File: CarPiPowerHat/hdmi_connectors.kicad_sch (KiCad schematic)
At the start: 2 parts, among them J1 HDMI_A_1.4, J6 1-84953-5

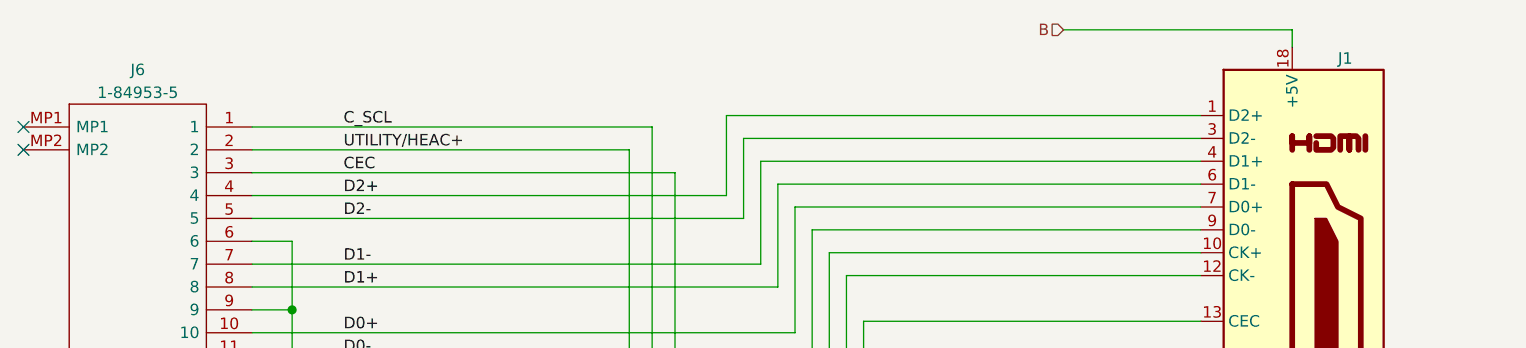
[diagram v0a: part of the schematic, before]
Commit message: updated layout
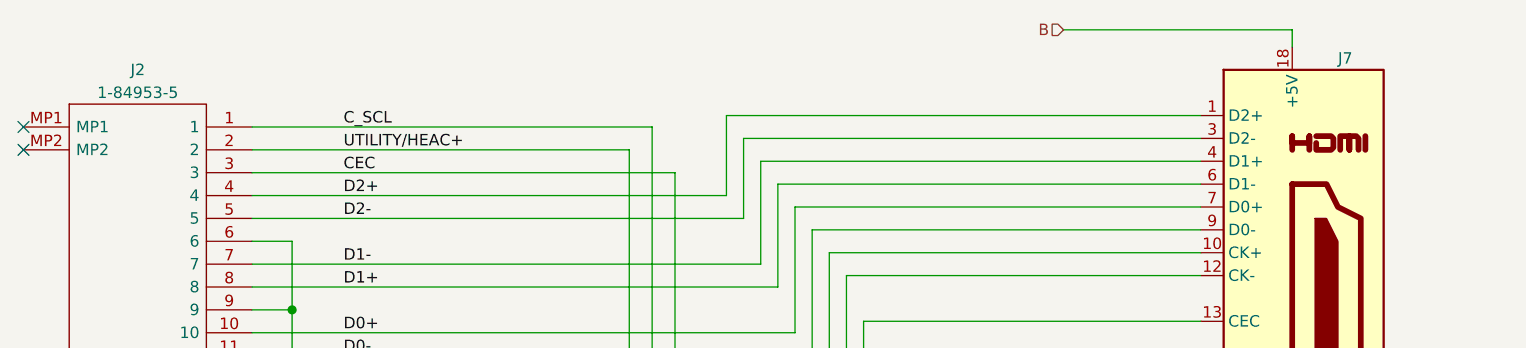
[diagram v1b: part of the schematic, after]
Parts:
- renumbered J6 to J2, J1 to J7
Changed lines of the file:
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@@
-(kicad_sch (version 20210126) (generator eeschema)
+(kicad_sch (version 20210406) (generator eeschema)
   (paper "A4")
   (junction (at 75.565 50.8) (diameter 1.016) (color 0 0 0 0))
@@
   (symbol (lib_id "power:GND") (at 75.565 77.47 0)
     (in_bom yes) (on_board yes)
-    (property "Reference" "#PWR0130" (id 0) (at 75.565 83.82 0)
+    (property "Reference" "#PWR0133" (id 0) (at 75.565 83.82 0)
       (effects (font (size 1.27 1.27)) hide)
     )
@@
   (symbol (lib_id "power:GND") (at 181.61 80.645 0)
     (in_bom yes) (on_board yes)
-    (property "Reference" "#PWR0106" (id 0) (at 181.61 86.995 0)
+    (property "Reference" "#PWR0134" (id 0) (at 181.61 86.995 0)
       (effects (font (size 1.27 1.27)) hide)
     )
@@
   (symbol (lib_id "power:GND") (at 202.565 80.645 0)
     (in_bom yes) (on_board yes)
-    (property "Reference" "#PWR0131" (id 0) (at 202.565 86.995 0)
+    (property "Reference" "#PWR0135" (id 0) (at 202.565 86.995 0)
       (effects (font (size 1.27 1.27)) hide)
     )
@@
   (symbol (lib_id "power:GND") (at 218.44 90.805 0)
     (in_bom yes) (on_board yes)
-    (property "Reference" "#PWR0132" (id 0) (at 218.44 97.155 0)
+    (property "Reference" "#PWR0136" (id 0) (at 218.44 97.155 0)
       (effects (font (size 1.27 1.27)) hide)
     )
@@
   (symbol (lib_id "1-84953-5:1-84953-5") (at 45.72 30.48 0)
     (in_bom yes) (on_board yes)
-    (property "Reference" "J6" (id 0) (at 58.42 24.13 0))
+    (property "Reference" "J2" (id 0) (at 58.42 24.13 0))
     (property "Value" "1-84953-5" (id 1) (at 58.42 26.67 0))
     (property "Footprint" "project_footprints:1849535" (id 2) (at 67.31 27.94 0)
@@
   (symbol (lib_id "CarPiPowerHat:HDMI_A_1.4") (at 186.69 49.53 0)
     (in_bom yes) (on_board yes)
-    (property "Reference" "J1" (id 0) (at 191.77 22.86 0)
+    (property "Reference" "J7" (id 0) (at 191.77 22.86 0)
       (effects (font (size 1.27 1.27)) (justify left))
     )

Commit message: Finished Layout
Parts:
- renumbered J7 to J1, J2 to J6
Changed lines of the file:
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@@
   (symbol (lib_id "power:GND") (at 75.565 77.47 0)
     (in_bom yes) (on_board yes)
-    (property "Reference" "#PWR0133" (id 0) (at 75.565 83.82 0)
+    (property "Reference" "#PWR0130" (id 0) (at 75.565 83.82 0)
       (effects (font (size 1.27 1.27)) hide)
     )
@@
   (symbol (lib_id "power:GND") (at 181.61 80.645 0)
     (in_bom yes) (on_board yes)
-    (property "Reference" "#PWR0134" (id 0) (at 181.61 86.995 0)
+    (property "Reference" "#PWR0106" (id 0) (at 181.61 86.995 0)
       (effects (font (size 1.27 1.27)) hide)
     )
@@
   (symbol (lib_id "power:GND") (at 202.565 80.645 0)
     (in_bom yes) (on_board yes)
-    (property "Reference" "#PWR0135" (id 0) (at 202.565 86.995 0)
+    (property "Reference" "#PWR0131" (id 0) (at 202.565 86.995 0)
       (effects (font (size 1.27 1.27)) hide)
     )
@@
   (symbol (lib_id "power:GND") (at 218.44 90.805 0)
     (in_bom yes) (on_board yes)
-    (property "Reference" "#PWR0136" (id 0) (at 218.44 97.155 0)
+    (property "Reference" "#PWR0132" (id 0) (at 218.44 97.155 0)
       (effects (font (size 1.27 1.27)) hide)
     )
@@
   (symbol (lib_id "1-84953-5:1-84953-5") (at 45.72 30.48 0)
     (in_bom yes) (on_board yes)
-    (property "Reference" "J2" (id 0) (at 58.42 24.13 0))
+    (property "Reference" "J6" (id 0) (at 58.42 24.13 0))
     (property "Value" "1-84953-5" (id 1) (at 58.42 26.67 0))
     (property "Footprint" "project_footprints:1849535" (id 2) (at 67.31 27.94 0)
@@
   (symbol (lib_id "CarPiPowerHat:HDMI_A_1.4") (at 186.69 49.53 0)
     (in_bom yes) (on_board yes)
-    (property "Reference" "J7" (id 0) (at 191.77 22.86 0)
+    (property "Reference" "J1" (id 0) (at 191.77 22.86 0)
       (effects (font (size 1.27 1.27)) (justify left))
     )

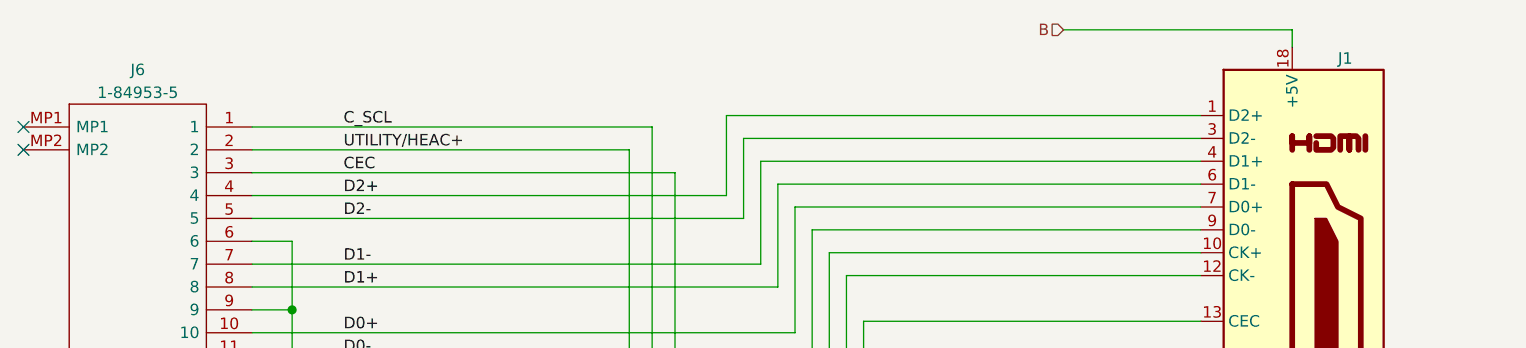
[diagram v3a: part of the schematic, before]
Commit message: Added part numbers
* Selected parts from lcsc
* Checked footprints
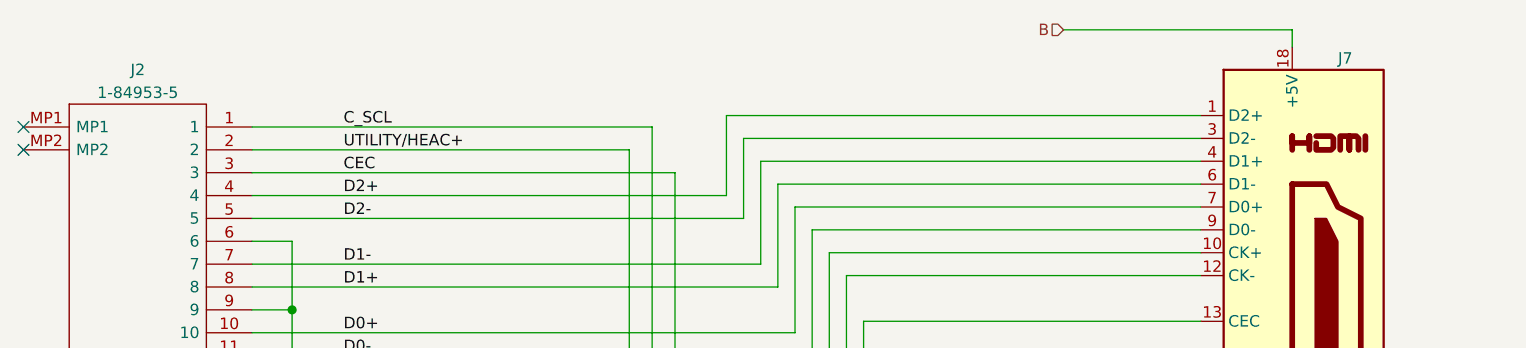
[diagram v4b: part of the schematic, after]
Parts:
- renumbered J6 to J2, J1 to J7
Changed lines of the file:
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@@
   (symbol (lib_id "power:GND") (at 75.565 77.47 0)
     (in_bom yes) (on_board yes)
-    (property "Reference" "#PWR0130" (id 0) (at 75.565 83.82 0)
+    (property "Reference" "#PWR0133" (id 0) (at 75.565 83.82 0)
       (effects (font (size 1.27 1.27)) hide)
     )
@@
   (symbol (lib_id "power:GND") (at 181.61 80.645 0)
     (in_bom yes) (on_board yes)
-    (property "Reference" "#PWR0106" (id 0) (at 181.61 86.995 0)
+    (property "Reference" "#PWR0134" (id 0) (at 181.61 86.995 0)
       (effects (font (size 1.27 1.27)) hide)
     )
@@
   (symbol (lib_id "power:GND") (at 202.565 80.645 0)
     (in_bom yes) (on_board yes)
-    (property "Reference" "#PWR0131" (id 0) (at 202.565 86.995 0)
+    (property "Reference" "#PWR0135" (id 0) (at 202.565 86.995 0)
       (effects (font (size 1.27 1.27)) hide)
     )
@@
   (symbol (lib_id "power:GND") (at 218.44 90.805 0)
     (in_bom yes) (on_board yes)
-    (property "Reference" "#PWR0132" (id 0) (at 218.44 97.155 0)
+    (property "Reference" "#PWR0136" (id 0) (at 218.44 97.155 0)
       (effects (font (size 1.27 1.27)) hide)
     )
@@
   (symbol (lib_id "1-84953-5:1-84953-5") (at 45.72 30.48 0)
     (in_bom yes) (on_board yes)
-    (property "Reference" "J6" (id 0) (at 58.42 24.13 0))
+    (property "Reference" "J2" (id 0) (at 58.42 24.13 0))
     (property "Value" "1-84953-5" (id 1) (at 58.42 26.67 0))
     (property "Footprint" "project_footprints:1849535" (id 2) (at 67.31 27.94 0)
@@
   (symbol (lib_id "CarPiPowerHat:HDMI_A_1.4") (at 186.69 49.53 0)
     (in_bom yes) (on_board yes)
-    (property "Reference" "J1" (id 0) (at 191.77 22.86 0)
+    (property "Reference" "J7" (id 0) (at 191.77 22.86 0)
       (effects (font (size 1.27 1.27)) (justify left))
     )

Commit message: Fixed some bugs, not done yet
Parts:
- renumbered J2 to J1, J7 to J5
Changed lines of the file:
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@@
   (symbol (lib_id "1-84953-5:1-84953-5") (at 45.72 30.48 0)
     (in_bom yes) (on_board yes)
-    (property "Reference" "J2" (id 0) (at 58.42 24.13 0))
+    (property "Reference" "J1" (id 0) (at 58.42 24.13 0))
     (property "Value" "1-84953-5" (id 1) (at 58.42 26.67 0))
     (property "Footprint" "project_footprints:1849535" (id 2) (at 67.31 27.94 0)
@@
   (symbol (lib_id "CarPiPowerHat:HDMI_A_1.4") (at 186.69 49.53 0)
     (in_bom yes) (on_board yes)
-    (property "Reference" "J7" (id 0) (at 191.77 22.86 0)
+    (property "Reference" "J5" (id 0) (at 191.77 22.86 0)
       (effects (font (size 1.27 1.27)) (justify left))
     )

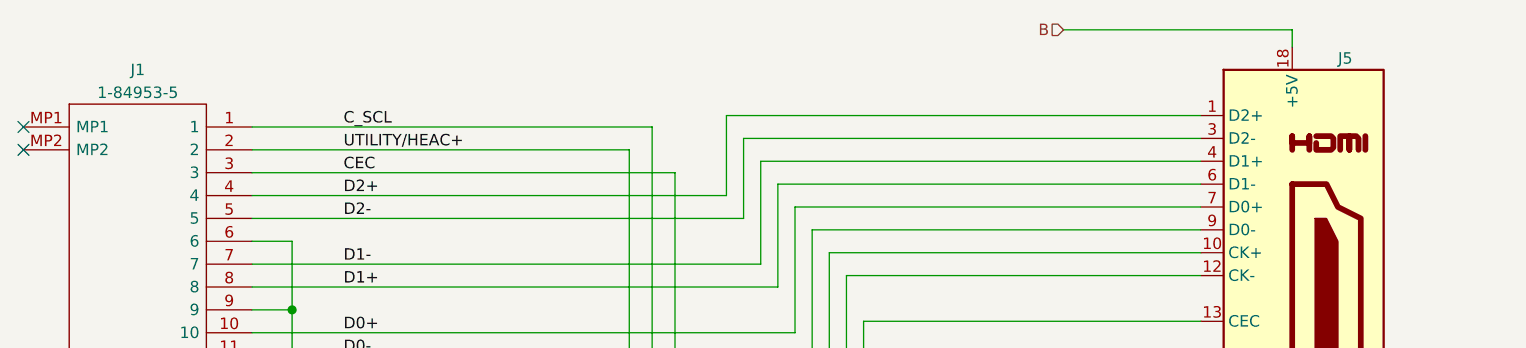
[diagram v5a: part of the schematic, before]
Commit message: Some rerouting
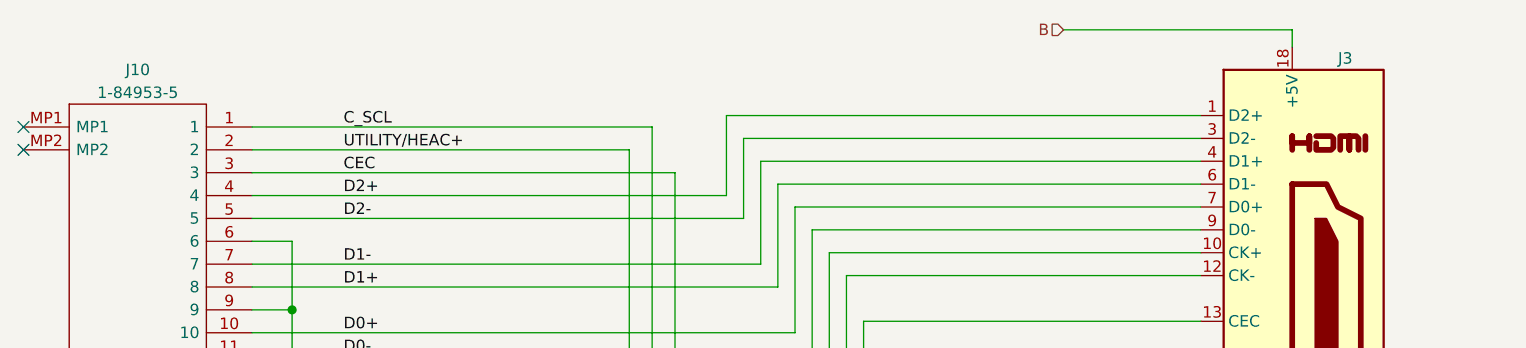
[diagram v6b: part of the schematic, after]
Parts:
- renumbered J1 to J10, J5 to J3
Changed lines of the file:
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@@
   (symbol (lib_id "power:GND") (at 75.565 77.47 0)
     (in_bom yes) (on_board yes)
-    (property "Reference" "#PWR0133" (id 0) (at 75.565 83.82 0)
+    (property "Reference" "#PWR0130" (id 0) (at 75.565 83.82 0)
       (effects (font (size 1.27 1.27)) hide)
     )
@@
   (symbol (lib_id "power:GND") (at 181.61 80.645 0)
     (in_bom yes) (on_board yes)
-    (property "Reference" "#PWR0134" (id 0) (at 181.61 86.995 0)
+    (property "Reference" "#PWR0106" (id 0) (at 181.61 86.995 0)
       (effects (font (size 1.27 1.27)) hide)
     )
@@
   (symbol (lib_id "power:GND") (at 202.565 80.645 0)
     (in_bom yes) (on_board yes)
-    (property "Reference" "#PWR0135" (id 0) (at 202.565 86.995 0)
+    (property "Reference" "#PWR0131" (id 0) (at 202.565 86.995 0)
       (effects (font (size 1.27 1.27)) hide)
     )
@@
   (symbol (lib_id "power:GND") (at 218.44 90.805 0)
     (in_bom yes) (on_board yes)
-    (property "Reference" "#PWR0136" (id 0) (at 218.44 97.155 0)
+    (property "Reference" "#PWR0132" (id 0) (at 218.44 97.155 0)
       (effects (font (size 1.27 1.27)) hide)
     )
@@
   (symbol (lib_id "1-84953-5:1-84953-5") (at 45.72 30.48 0)
     (in_bom yes) (on_board yes)
-    (property "Reference" "J1" (id 0) (at 58.42 24.13 0))
+    (property "Reference" "J10" (id 0) (at 58.42 24.13 0))
     (property "Value" "1-84953-5" (id 1) (at 58.42 26.67 0))
     (property "Footprint" "project_footprints:1849535" (id 2) (at 67.31 27.94 0)
@@
   (symbol (lib_id "CarPiPowerHat:HDMI_A_1.4") (at 186.69 49.53 0)
     (in_bom yes) (on_board yes)
-    (property "Reference" "J5" (id 0) (at 191.77 22.86 0)
+    (property "Reference" "J3" (id 0) (at 191.77 22.86 0)
       (effects (font (size 1.27 1.27)) (justify left))
     )

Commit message: Finalized 2.2
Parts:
- renumbered J10 to J1, J3 to J5
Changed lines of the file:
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@@
   (symbol (lib_id "power:GND") (at 75.565 77.47 0)
     (in_bom yes) (on_board yes)
-    (property "Reference" "#PWR0130" (id 0) (at 75.565 83.82 0)
+    (property "Reference" "#PWR0133" (id 0) (at 75.565 83.82 0)
       (effects (font (size 1.27 1.27)) hide)
     )
@@
   (symbol (lib_id "power:GND") (at 181.61 80.645 0)
     (in_bom yes) (on_board yes)
-    (property "Reference" "#PWR0106" (id 0) (at 181.61 86.995 0)
+    (property "Reference" "#PWR0134" (id 0) (at 181.61 86.995 0)
       (effects (font (size 1.27 1.27)) hide)
     )
@@
   (symbol (lib_id "power:GND") (at 202.565 80.645 0)
     (in_bom yes) (on_board yes)
-    (property "Reference" "#PWR0131" (id 0) (at 202.565 86.995 0)
+    (property "Reference" "#PWR0135" (id 0) (at 202.565 86.995 0)
       (effects (font (size 1.27 1.27)) hide)
     )
@@
   (symbol (lib_id "power:GND") (at 218.44 90.805 0)
     (in_bom yes) (on_board yes)
-    (property "Reference" "#PWR0132" (id 0) (at 218.44 97.155 0)
+    (property "Reference" "#PWR0136" (id 0) (at 218.44 97.155 0)
       (effects (font (size 1.27 1.27)) hide)
     )
@@
   (symbol (lib_id "1-84953-5:1-84953-5") (at 45.72 30.48 0)
     (in_bom yes) (on_board yes)
-    (property "Reference" "J10" (id 0) (at 58.42 24.13 0))
+    (property "Reference" "J1" (id 0) (at 58.42 24.13 0))
     (property "Value" "1-84953-5" (id 1) (at 58.42 26.67 0))
     (property "Footprint" "project_footprints:1849535" (id 2) (at 67.31 27.94 0)
@@
   (symbol (lib_id "CarPiPowerHat:HDMI_A_1.4") (at 186.69 49.53 0)
     (in_bom yes) (on_board yes)
-    (property "Reference" "J3" (id 0) (at 191.77 22.86 0)
+    (property "Reference" "J5" (id 0) (at 191.77 22.86 0)
       (effects (font (size 1.27 1.27)) (justify left))
     )

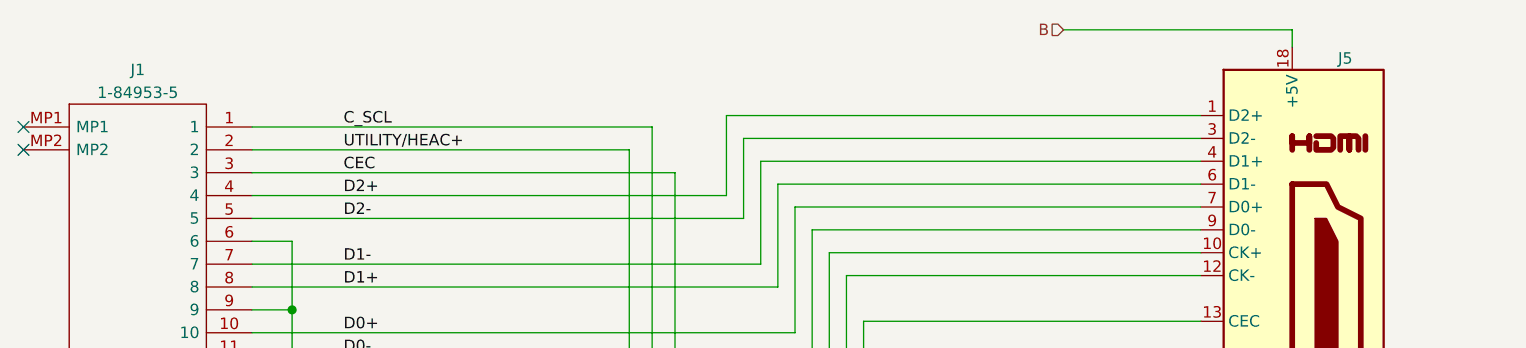
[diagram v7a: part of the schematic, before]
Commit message: Finalizing, checking parts
Might be ready for production
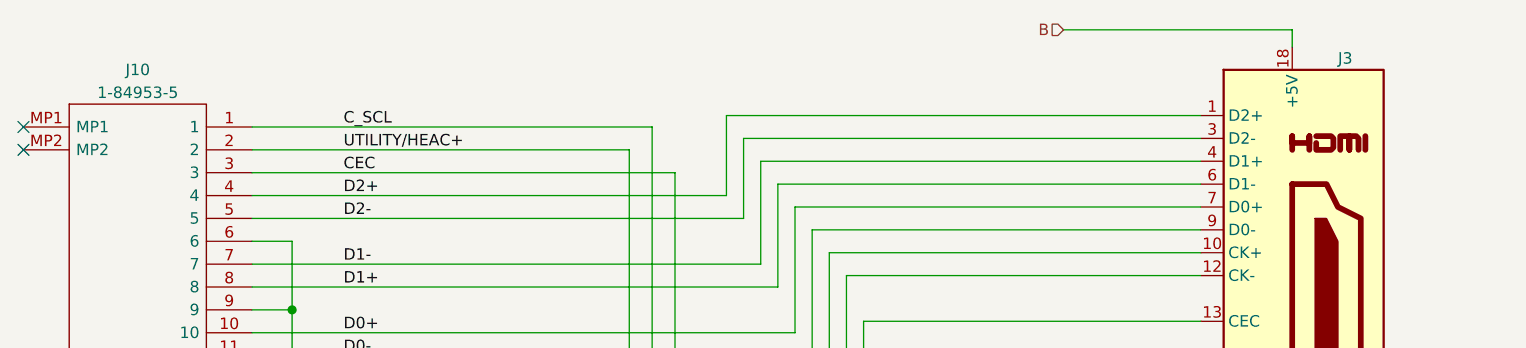
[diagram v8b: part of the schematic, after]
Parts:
- J10: renamed from J1; footprint project_footprints:1849535 -> SamacSys_Parts:1849535
- renumbered J5 to J3
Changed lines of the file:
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@@
   (symbol (lib_id "1-84953-5:1-84953-5") (at 45.72 30.48 0)
     (in_bom yes) (on_board yes)
-    (property "Reference" "J1" (id 0) (at 58.42 24.13 0))
+    (property "Reference" "J10" (id 0) (at 58.42 24.13 0))
     (property "Value" "1-84953-5" (id 1) (at 58.42 26.67 0))
-    (property "Footprint" "project_footprints:1849535" (id 2) (at 67.31 27.94 0)
+    (property "Footprint" "SamacSys_Parts:1849535" (id 2) (at 67.31 27.94 0)
       (effects (font (size 1.27 1.27)) (justify left) hide)
     )
@@
   (symbol (lib_id "CarPiPowerHat:HDMI_A_1.4") (at 186.69 49.53 0)
     (in_bom yes) (on_board yes)
-    (property "Reference" "J5" (id 0) (at 191.77 22.86 0)
+    (property "Reference" "J3" (id 0) (at 191.77 22.86 0)
       (effects (font (size 1.27 1.27)) (justify left))
     )
